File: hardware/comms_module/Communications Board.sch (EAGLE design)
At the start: 22 parts, among them U2 STC3115

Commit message: Add MUXes and moisture detection schematics.
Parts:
- added MCU: SABLE-X-BLE-MODULE, Capstone Library:SABLE-X-BLE-MODULE
- added MUX1: 74LV4051, Capstone Library:74LV4051
- added MUX2, U$3: 74LVC2G53, Capstone Library:74LVC2G53
- added Q1: MOSFET-PCHANNEL, SparkFun-DiscreteSemi:MOSFET-PCHANNEL
- added R1, R13, R14, R3: 4K32_0.1%, SparkFun-Passives:RESISTOR0603-RES
- U$1: value SABLE-X-BLE-MODULE -> 74LV4051; device Capstone Library:SABLE-X-BLE-MODULE -> Capstone Library:74LV4051
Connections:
- new net +1V3: MCU.DIO12, R14.1, R3.1
- new net +3V3: MCU.VCC, Q1.D
- new net BANDAGE_A_0: MCU.DIO11, MUX1.Y0, U$1.Y0
- new net BANDAGE_A_1: MUX1.Y1, U$1.Y1
- new net BANDAGE_A_2: MUX1.Y2, U$1.Y2
- new net BANDAGE_A_3: MUX1.Y3, U$1.Y3
- new net BANDAGE_A_4: MUX1.Y4, U$1.Y4
- new net BANDAGE_ID_0: U$1.Y5
- new net BANDAGE_ID_1: U$1.Y6
- new net CONN_STATE_RD: MCU.DIO4, MUX1.Z, MUX2.Z, U$1.Z, U$3.Z
- new net DBG_LED: U$1.Y7
- new net JTAG_TCKC: MCU.TCKC
- new net JTAG_TDI: MCU.DIO6/TDI
- new net JTAG_TDO: MCU.DIO5/TDO
- new net JTAG_TSMC: MCU.TSMC
- new net MCU_RST: MCU.RESET
- new net MPSW: MCU.DIO_0/BOOT_TX, MUX2.S, U$3.S
- new net MP_EN_SW: MCU.DIO9, MUX2./E, U$3./E
- new net MSW_0: MCU.DIO10, MUX1.S0, U$1.S0
- new net MSW_1: MCU.DIO8, MUX1.S1, U$1.S1
- new net MSW_2: MCU.DIO7, MUX1.S2, U$1.S2
- new net N$11: U$1.VEE
- new net PERIPHERAL_PWR: MCU.DIO1/BOOT_RX, Q1.G
- new net PERIPHERAL_VCC: MUX1.VCC, MUX2.VCC, Q1.S, R1.1, R13.1, U$1.VCC, U$3.VCC
- new net VSENSE_0: MCU.DIO14, MUX2.Y1, R1.2, R13.2, U$3.Y1
- new net VSENSE_1: MCU.DIO13, MUX2.Y0, R14.2, R3.2, U$3.Y0
- net GND: now also MCU.GND, MUX1./E, MUX1.GND, MUX1.VEE, MUX2.GND, U$1./E, U$1.GND, U$3.GND
- net SCL: now also MCU.DIO2
- net SDA: now also MCU.DIO3
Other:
- note added: "Close to R3"
- note added: "THIS MOSFET NOT YET SELECTED. VERIFY PKG."
- note added: "TP1"

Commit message: Add power management components.
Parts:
- removed MUX1: 74LV4051, Capstone Library:74LV4051
- removed MUX2: 74LVC2G53, Capstone Library:74LVC2G53
- removed R13, R14: 4K32_0.1%, SparkFun-Passives:RESISTOR0603-RES
- added C1, C3, C7, C8: (no value), SparkFun-Passives:CAP0603-CAP
- added L1: 1.5uH, SparkFun-Passives:INDUCTOR
- added U$4: TPS63031, Capstone Library:TPS63031
- added U$5: TLV717P, Capstone Library:TLV717P
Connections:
- new net N$10: C3.1, U$4.EN, U$4.PS/SYNC, U$4.VINA
- new net N$5: L1.1, U$4.L1
- new net N$8: L1.2, U$4.L2
- net +1V3: now also C8.1, U$5.VOUT; no longer R14.1
- net +3V3: now also C7.1, U$4.FB, U$4.VOUT
- net BANDAGE_A_0: no longer MUX1.Y0
- net BANDAGE_A_1: no longer MUX1.Y1
- net BANDAGE_A_2: no longer MUX1.Y2
- net BANDAGE_A_3: no longer MUX1.Y3
- net BANDAGE_A_4: no longer MUX1.Y4
- net CONN_STATE_RD: no longer MUX1.Z, MUX2.Z
- net GND: now also C1.2, C3.2, C7.2, C8.2, U$4.GND, U$4.PGND, U$5.GND; no longer MUX1./E, MUX1.GND, MUX1.VEE, MUX2.GND
- net MPSW: no longer MUX2.S
- net MP_EN_SW: no longer MUX2./E
- net MSW_0: no longer MUX1.S0
- net MSW_1: no longer MUX1.S1
- net MSW_2: no longer MUX1.S2
- net PERIPHERAL_VCC: now also U$5.EN, U$5.IN; no longer MUX1.VCC, MUX2.VCC, R13.1
- net VSENSE_0: no longer MUX2.Y1, R13.2
- net VSENSE_1: no longer MUX2.Y0, R14.2
- net V_PREBUCK: now also C1.1, U$4.VIN
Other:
- note added: "1V3 Regulator"
- note added: "3V3 Regulator"
- note added: "L1 not yet selected."
- note added: "Layout from TI Reference Design"
- note added: "Peripheral Power Disable"
- note added: "Place IN close to 3V3 reg."
- note removed: "TP1"
- moved on the sheet: MCU, Q1

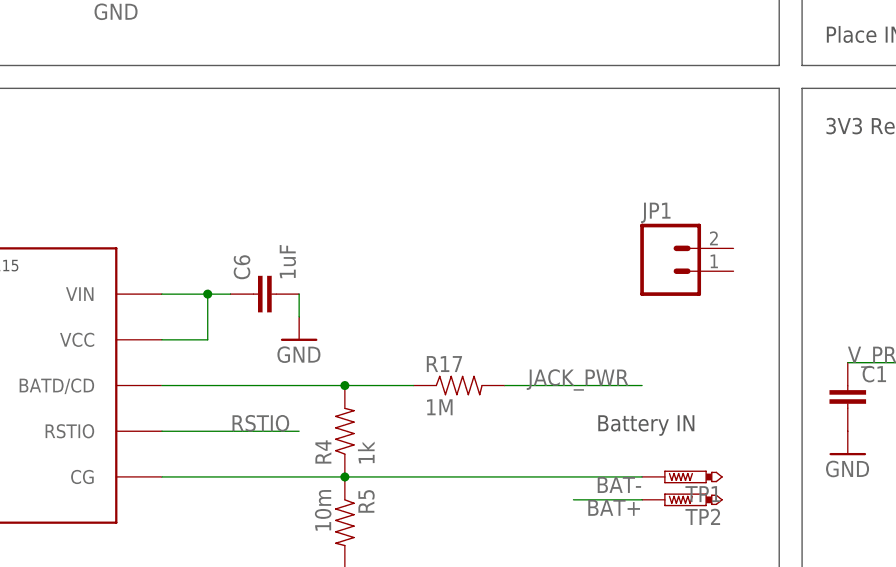
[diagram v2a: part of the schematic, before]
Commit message: Fix STC3115 Vcc connection
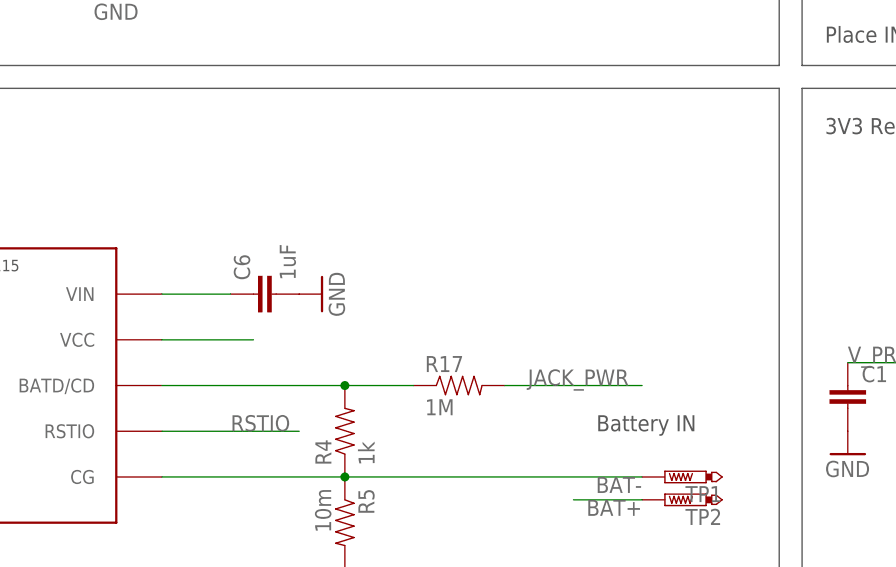
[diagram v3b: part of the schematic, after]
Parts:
- removed JP1: (no value), SparkFun-Connectors:M02JST-PTH-VERT
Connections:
- net N$6: no longer U2.VCC
- net VCC: now also U2.VCC
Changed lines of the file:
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@@
 <part name="SJ1" library="jumper" deviceset="SJ" device=""/>
 <part name="MCU" library="Capstone Library" deviceset="SABLE-X-BLE-MODULE" device=""/>
-<part name="JP1" library="SparkFun-Connectors" deviceset="M02" device="JST-PTH-VERT"/>
 <part name="TP1" library="testpad" deviceset="PTR1" device="TP16SQ"/>
 <part name="TP2" library="testpad" deviceset="PTR1" device="TP16SQ"/>
@@
 <instance part="GND15" gate="1" x="27.94" y="15.24"/>
 <instance part="C6" gate="G$1" x="78.74" y="40.64" rot="R90"/>
-<instance part="GND16" gate="1" x="81.28" y="35.56"/>
+<instance part="GND16" gate="1" x="83.82" y="40.64" rot="R90"/>
 <instance part="R4" gate="G$1" x="86.36" y="25.4" rot="R90"/>
 <instance part="R5" gate="G$1" x="86.36" y="15.24" rot="R270"/>
@@
 <instance part="SJ1" gate="1" x="25.4" y="106.68"/>
 <instance part="MCU" gate="G$1" x="353.06" y="116.84"/>
-<instance part="JP1" gate="G$1" x="121.92" y="43.18"/>
 <instance part="TP1" gate="G$1" x="121.92" y="20.32" rot="R90"/>
 <instance part="TP2" gate="G$1" x="121.92" y="17.78" rot="R90"/>
@@
 <pinref part="C6" gate="G$1" pin="2"/>
 <pinref part="GND16" gate="1" pin="GND"/>
-<wire x1="81.28" y1="38.1" x2="81.28" y2="40.64" width="0.1524" layer="91"/>
 </segment>
 <segment>
@@
 <net name="N$6" class="0">
 <segment>
-<pinref part="U2" gate="G$1" pin="VCC"/>
-<wire x1="66.04" y1="35.56" x2="71.12" y2="35.56" width="0.1524" layer="91"/>
-<wire x1="71.12" y1="35.56" x2="71.12" y2="40.64" width="0.1524" layer="91"/>
 <pinref part="U2" gate="G$1" pin="VIN"/>
-<wire x1="66.04" y1="40.64" x2="71.12" y2="40.64" width="0.1524" layer="91"/>
+<wire x1="66.04" y1="40.64" x2="73.66" y2="40.64" width="0.1524" layer="91"/>
 <pinref part="C6" gate="G$1" pin="1"/>
-<junction x="71.12" y="40.64"/>
-<wire x1="71.12" y1="40.64" x2="73.66" y2="40.64" width="0.1524" layer="91"/>
 </segment>
 </net>
@@
 <pinref part="P+1" gate="VCC" pin="VCC"/>
 </segment>
-</net>
+<segment>
+<pinref part="U2" gate="G$1" pin="VCC"/>
+<wire x1="66.04" y1="35.56" x2="76.2" y2="35.56" width="0.1524" layer="91"/>
+</segment>
+</net>

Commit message: Add remaining components and start board layout.
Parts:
- removed Q1: MOSFET-PCHANNEL, SparkFun-DiscreteSemi:MOSFET-PCHANNEL
- removed R10, R9: 1k, SparkFun-Passives:RESISTOR0603-RES
- removed SJ1: (no value), jumper:SJ
- added C10: 10uF, SparkFun-Passives:CAP0603-CAP
- added C9: 1uF, SparkFun-Passives:CAP0603-CAP
- added JP1, JP2: (no value), SparkFun-Connectors:M05X2NO_SILK
- added PSW: (no value), Capstone Library:SWITCH-SPDT
- added R13: 1Meg, SparkFun-Passives:RESISTOR0603-RES
- added R14, R16, R18: 100Meg, SparkFun-Passives:RESISTOR0603-RES
- added R15, R19: 10k, SparkFun-Passives:RESISTOR0603-RES
- added U$6, U$7, U$8: DMC2990UDJ, Capstone Library:DMC2990UDJ
- added X2: USB-MICROB, SparkFun:USB-MICROB
- C1, C7: value (none) -> 10uF
- C3: value (none) -> 0.1uF
- L1: device SparkFun-Passives:INDUCTOR -> Capstone Library:INDUCTOR
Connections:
- net BANDAGE_ID_0 renamed BANDAGE_DETECT
- removed net BANDAGE_ID_1: U$1.Y6
- removed net N$17: R9.1, U$2.PGOOD
- removed net N$18: R10.1, U$2.CHG
- removed net RSTIO: U2.RSTIO
- new net /SYSDISBL: C9.1, R15.1, U$1.Y6
- new net AGND: JP1.5, JP2.5
- new net BATDC: R17.1, R4.2, R6.2, U2.BATD/CD
- new net N$12: R13.1, U$6G$2.D
- new net N$13: JP1.8
- new net N$14: R14.1, R15.2, U$6G$2.G
- new net N$15: JP1.6
- new net N$16: JP1.3
- new net N$21: R16.2, U$7G$1.D
- new net N$22: R18.2, R19.2, U$6G$2.S, U$7G$1.G, U$7G$2.G
- new net N$25: JP2.9
- new net N$26: JP2.8
- new net N$27: JP2.6
- new net N$28: JP2.3
- new net N$29: JP2.1
- new net N$9: R13.2, U$6G$1.D, U$6G$1.G
- new net SYSOFF: R16.1, R6.1, U$2.SYSOFF, U$7G$2.D
- net +3V3: now also C10.1, R19.1, U$8G$2.S, U2.VCC; no longer Q1.D
- net BAT+: now also C6.1, PSW.P, R17.2, R18.1, U$7G$2.S, U2.VIN; no longer TP2.TP
- net BAT-: now also C5.2
- net GND: now also C10.2, C9.2, JP1.7, JP2.7, R14.2, U$6G$1.S, U$7G$1.S, X2.GND; no longer C5.2, R6.1
- net JACK_PWR: now also X2.VBUS; no longer R17.2, SJ1.1
- net MCU_RST: now also U2.RSTIO
- net N$19: now also JP1.1; no longer R6.2, SJ1.2, U$2.SYSOFF
- net N$6: now also PSW.S, TP2.TP; no longer C6.1, U2.VIN
- net N$7: now also JP1.9; no longer R17.1, R4.2, U2.BATD/CD
- net PERIPHERAL_PWR: now also U$8G$2.G; no longer Q1.G
- net PERIPHERAL_VCC: now also JP1.10, JP2.10, U$8G$2.D; no longer Q1.S
- net SCL: now also JP1.2, JP2.2
- net SDA: now also JP1.4, JP2.4
- net VCC: no longer U2.VCC
- net V_PREBUCK: no longer R10.2, R9.2
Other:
- note added: "ADD CHG/PGOOD LEDs if space Available"
- note added: "Battery Power Disable"
- note removed: "L1 not yet selected."
- note removed: "THIS MOSFET NOT YET SELECTED. VERIFY PKG."
- moved on the sheet: C6, MCU, R6, TP2

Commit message: Continued routing of the communications board.
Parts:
- removed PSW: (no value), Capstone Library:SWITCH-SPDT
- removed TP1, TP2: PTR1TP16SQ, testpad:PTR1TP16SQ
- added B_CONN, B_EN: (no value), SparkFun-Connectors:M02PTH
- added JP3, JP4: (no value), SparkFun-Connectors:M021X02_NO_SILK
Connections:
- removed net N$6: PSW.S, TP2.TP
- new net B+IN: B_CONN.1, B_EN.1
- net +3V3: now also JP3.1, JP4.1
- net BAT+: now also B_EN.2; no longer PSW.P
- net BAT-: now also B_CONN.2; no longer TP1.TP
- net V_PREBUCK: now also JP3.2, JP4.2
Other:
- note added: "Top-Bottom Board Power Passthrough"
- note removed: "Battery IN"
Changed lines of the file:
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@@
 <part name="R17" library="SparkFun-Passives" deviceset="RESISTOR" device="0603-RES" value="1M"/>
 <part name="MCU" library="Capstone Library" deviceset="SABLE-X-BLE-MODULE" device=""/>
-<part name="TP1" library="testpad" deviceset="PTR1" device="TP16SQ"/>
-<part name="TP2" library="testpad" deviceset="PTR1" device="TP16SQ"/>
 <part name="+3V1" library="supply1" deviceset="+3V3" device=""/>
 <part name="GND1" library="supply1" deviceset="GND" device=""/>
@@
 <part name="+3V4" library="supply1" deviceset="+3V3" device=""/>
 <part name="+3V5" library="supply1" deviceset="+3V3" device=""/>
-<part name="PSW" library="Capstone Library" deviceset="SWITCH-SPDT" device=""/>
 <part name="JP1" library="SparkFun-Connectors" deviceset="M05X2" device="NO_SILK"/>
 <part name="GND3" library="supply1" deviceset="GND" device=""/>
@@
 <part name="X2" library="SparkFun" deviceset="USB" device="-MICROB"/>
 <part name="GND22" library="SparkFun" deviceset="GND" device=""/>
+<part name="B_EN" library="SparkFun-Connectors" deviceset="M02" device="PTH"/>
+<part name="B_CONN" library="SparkFun-Connectors" deviceset="M02" device="PTH"/>
+<part name="JP3" library="SparkFun-Connectors" deviceset="M02" device="1X02_NO_SILK"/>
+<part name="+3V6" library="supply1" deviceset="+3V3" device=""/>
+<part name="JP4" library="SparkFun-Connectors" deviceset="M02" device="1X02_NO_SILK"/>
+<part name="+3V7" library="supply1" deviceset="+3V3" device=""/>
 </parts>
 <sheets>
@@
 <wire x1="134.62" y1="167.64" x2="83.82" y2="167.64" width="0.1524" layer="97"/>
 <text x="86.36" y="198.12" size="1.778" layer="97">I2C Pullups</text>
-<text x="114.3" y="22.86" size="1.778" layer="97">Battery IN</text>
 <text x="147.32" y="190.5" size="1.778" layer="97">Next steps:
  - Make the component for the buck/boost
@@
 <text x="236.22" y="81.28" size="1.778" layer="97">Battery Power Disable </text>
 <text x="35.56" y="139.7" size="1.778" layer="97">ADD CHG/PGOOD LEDs if space Available</text>
+<text x="360.68" y="50.8" size="1.778" layer="97">Top-Bottom Board Power Passthrough</text>
 </plain>
 <instances>
@@
 <instance part="R17" gate="G$1" x="99.06" y="30.48"/>
 <instance part="MCU" gate="G$1" x="320.04" y="172.72"/>
-<instance part="TP1" gate="G$1" x="121.92" y="20.32" rot="R90"/>
-<instance part="TP2" gate="G$1" x="124.46" y="10.16" rot="R90"/>
 <instance part="+3V1" gate="G$1" x="259.08" y="193.04"/>
 <instance part="GND1" gate="1" x="259.08" y="182.88"/>
@@
 <instance part="+3V4" gate="G$1" x="236.22" y="66.04" rot="R90"/>
 <instance part="+3V5" gate="G$1" x="83.82" y="35.56" rot="R270"/>
-<instance part="PSW" gate="1" x="114.3" y="12.7"/>
 <instance part="JP1" gate="G$1" x="378.46" y="20.32"/>
 <instance part="GND3" gate="1" x="360.68" y="12.7"/>
@@
 <instance part="X2" gate="G$1" x="10.16" y="81.28" rot="R180"/>
 <instance part="GND22" gate="1" x="38.1" y="78.74"/>
+<instance part="B_EN" gate="G$1" x="114.3" y="12.7" rot="R180"/>
+<instance part="B_CONN" gate="G$1" x="127" y="22.86" rot="R180"/>
+<instance part="JP3" gate="G$1" x="375.92" y="40.64"/>
+<instance part="+3V6" gate="G$1" x="406.4" y="40.64" rot="R270"/>
+<instance part="JP4" gate="G$1" x="464.82" y="40.64"/>
+<instance part="+3V7" gate="G$1" x="495.3" y="40.64" rot="R270"/>
 </instances>
 <busses>
@@
 <label x="142.24" y="33.02" size="1.778" layer="95"/>
 </segment>
+<segment>
+<pinref part="JP3" gate="G$1" pin="2"/>
+<wire x1="383.54" y1="43.18" x2="398.78" y2="43.18" width="0.1524" layer="91"/>
+<label x="383.54" y="43.18" size="1.778" layer="95"/>
+</segment>
+<segment>
+<pinref part="JP4" gate="G$1" pin="2"/>
+<wire x1="472.44" y1="43.18" x2="487.68" y2="43.18" width="0.1524" layer="91"/>
+<label x="472.44" y="43.18" size="1.778" layer="95"/>
+</segment>
 </net>
 <net name="JACK_PWR" class="0">
@@
 </segment>
 <segment>
-<pinref part="PSW" gate="1" pin="P"/>
-<wire x1="111.76" y1="12.7" x2="106.68" y2="12.7" width="0.1524" layer="91"/>
-<label x="106.68" y="12.7" size="1.778" layer="95"/>
+<pinref part="B_EN" gate="G$1" pin="2"/>
+<wire x1="106.68" y1="10.16" x2="96.52" y2="10.16" width="0.1524" layer="91"/>
+<label x="96.52" y="10.16" size="1.778" layer="95"/>
 </segment>
 </net>
@@
 <net name="BAT-" class="0">
 <segment>
-<label x="106.68" y="17.78" size="1.778" layer="95"/>
+<label x="106.68" y="20.32" size="1.778" layer="95"/>
 <pinref part="R4" gate="G$1" pin="1"/>
 <pinref part="U2" gate="G$1" pin="CG"/>
@@
 <junction x="86.36" y="20.32"/>
 <wire x1="119.38" y1="20.32" x2="86.36" y2="20.32" width="0.1524" layer="91"/>
-<pinref part="TP1" gate="G$1" pin="TP"/>
+<pinref part="B_CONN" gate="G$1" pin="2"/>
 </segment>
 <segment>
@@
 <pinref part="+3V5" gate="G$1" pin="+3V3"/>
 </segment>
+<segment>
+<pinref part="JP3" gate="G$1" pin="1"/>
+<wire x1="383.54" y1="40.64" x2="403.86" y2="40.64" width="0.1524" layer="91"/>
+<pinref part="+3V6" gate="G$1" pin="+3V3"/>
+<label x="383.54" y="40.64" size="1.778" layer="95"/>
+</segment>
+<segment>
+<pinref part="JP4" gate="G$1" pin="1"/>
+<wire x1="472.44" y1="40.64" x2="492.76" y2="40.64" width="0.1524" layer="91"/>
+<pinref part="+3V7" gate="G$1" pin="+3V3"/>
+<label x="472.44" y="40.64" size="1.778" layer="95"/>
+</segment>
 </net>
 <net name="MCU_RST" class="0">
@@
 </segment>
 </net>
-<net name="N$6" class="0">
-<segment>
-<pinref part="PSW" gate="1" pin="S"/>
-<pinref part="TP2" gate="G$1" pin="TP"/>
-<wire x1="119.38" y1="10.16" x2="121.92" y2="10.16" width="0.1524" layer="91"/>
-</segment>
-</net>
+<net name="B+IN" class="0">
+<segment>
+<pinref part="B_CONN" gate="G$1" pin="1"/>
+<wire x1="119.38" y1="22.86" x2="106.68" y2="22.86" width="0.1524" layer="91"/>
+<label x="106.68" y="22.86" size="1.778" layer="95"/>
+</segment>
+<segment>
+<pinref part="B_EN" gate="G$1" pin="1"/>
+<wire x1="106.68" y1="12.7" x2="96.52" y2="12.7" width="0.1524" layer="91"/>
+<label x="96.52" y="12.7" size="1.778" layer="95"/>
+</segment>
+</net>

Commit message: Continued routing of top and bottom.
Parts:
- added JP5, JP6: (no value), SparkFun-Connectors:M01PTH
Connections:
- removed net N$11: U$1.VEE
- removed net N$13: JP1.8
- removed net N$14: R14.1, R15.2, U$6G$2.G
- removed net N$15: JP1.6
- removed net N$16: JP1.3
- removed net N$19: JP1.1
- removed net N$7: JP1.9
- removed net VCC: R11.2, R12.2
- new net SYSDPASS: JP5.1, JP6.1, R14.1, R15.2, U$6G$2.G
- net +3V3: now also R11.2, R12.2
- net BANDAGE_A_0: now also JP1.6
- net BANDAGE_A_1: now also JP1.3
- net BANDAGE_A_2: now also JP1.8
- net BANDAGE_A_3: now also JP1.1
- net BANDAGE_A_4: now also JP1.9
- net GND: now also U$1.VEE
- net MSW_0: now also MCU.DIO7; no longer MCU.DIO10
- net MSW_2: now also MCU.DIO10; no longer MCU.DIO7
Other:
- moved on the sheet: R13, R16, R18, R6, U$6G$1, U$6G$2, U$7G$1, U$7G$2

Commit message: Convert to 4 layer. Nearly complete routing.
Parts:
- removed JP1, JP2: (no value), SparkFun-Connectors:M05X2NO_SILK
- removed MCU: SABLE-X-BLE-MODULE, Capstone Library:SABLE-X-BLE-MODULE
- added C11, C12: 1.2pF, SparkFun-Passives:CAP0402-CAP
- added C13, C23, C24: 12pF, SparkFun-Passives:CAP0402-CAP
- added C14: 1uF, SparkFun-Passives:CAP0402-CAP
- added C15, C16, C17, C19, C21, C22: 100nF, SparkFun-Passives:CAP0402-CAP
- added C18, C20: 10uF, SparkFun-Passives:CAP0402-CAP
- added FL1: BLM18HE152SN1, Michael Blouin Library:INDUCTOR0603
- added JP7, JP8: 2X6 FEMALE, SparkFun-Connectors:M06X2PTH_FEMALE
- added L2: 2nH, SparkFun-Passives:INDUCTOR0402
- added L3: 15nH, SparkFun-Passives:INDUCTOR0402
- added L4: 10uH, Michael Blouin Library:INDUCTOR0603
- added R9: 100k, SparkFun-Passives:RESISTOR0603-RES
- added U1: Value, Capstone Library:CC2640F128RHBR
- added Y1: 32.768kHz, Capstone Library:CRYSTAL
- added Y2: 24MHz, Capstone Library:CRYSTAL-GROUNDED
- C1, C3, C7, C8: device SparkFun-Passives:CAP0603-CAP -> SparkFun-Passives:CAP0402-CAP
- R1, R3: device SparkFun-Passives:RESISTOR0603-RES -> SparkFun-Passives:RESISTOR0402-RES
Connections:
- removed net BANDAGE_DETECT: U$1.Y5
- removed net SYSDPASS: JP5.1, JP6.1, R14.1, R15.2, U$6G$2.G
- new net ANTENNA: C13.2
- new net DCDC_SW: L4.1, U1.DCDC_SW
- new net N$18: C23.1, U1.X32K_Q2, Y1.1
- new net N$19: C24.1, U1.X32K_Q1, Y1.2
- new net N$41: C12.1, C13.1, L2.2
- new net N$43: C14.1, U1.DCOUPL
- new net PERIPHERAL_DETECT: JP7.12, JP8.12, U$1.Y5
- new net RF_N: L3.1, U1.RF_N
- new net RF_P: C11.1, L2.1, L3.2, U1.RF_P
- new net VCC: C16.1, C17.1, C18.1, C19.1, FL1.2, R9.2, U1.VDDS, U1.VDDS2, U1.VDDS_DCDC
- new net VDDR: C20.1, C21.1, C22.1, L4.2, U1.VDDR, U1.VDDR_RF
- new net X24M_N: U1.X24M_N, Y2.2
- new net X24M_P: U1.X24M_P, Y2.1
- net +1V3: now also U1.DIO_9; no longer MCU.DIO12
- net +3V3: now also FL1.1; no longer MCU.VCC
- net /SYSDISBL: now also JP5.1, JP6.1, R14.1, R15.2, U$6G$2.G
- net AGND: now also JP8.5; no longer JP1.5, JP2.5
- net BANDAGE_A_0: now also JP7.6, U$1.Y3, U1.DIO_10; no longer JP1.6, MCU.DIO11, U$1.Y0
- net BANDAGE_A_1: now also JP7.3, U$1.Y2; no longer JP1.3, U$1.Y1
- net BANDAGE_A_2: now also JP7.8, U$1.Y1; no longer JP1.8, U$1.Y2
- net BANDAGE_A_3: now also JP7.1, U$1.Y0; no longer JP1.1, U$1.Y3
- net BANDAGE_A_4: now also JP7.9; no longer JP1.9
- net CONN_STATE_RD: now also U1.DIO_12; no longer MCU.DIO4
- net GND: now also C11.2, C12.2, C14.2, C15.2, C16.2, C17.2, C18.2, C19.2, C20.2, C21.2, C22.2, C23.2, C24.2, JP7.5, JP7.7, JP8.7, U1.VSS, Y2.3; no longer JP1.7, JP2.7, MCU.GND
- net JTAG_TCKC: now also U1.JTAG_TCKC; no longer MCU.TCKC
- net JTAG_TDI: now also U1.DIO_6; no longer MCU.DIO6/TDI
- net JTAG_TDO: now also U1.DIO_5; no longer MCU.DIO5/TDO
- net JTAG_TSMC: now also U1.JTAG_TMSC; no longer MCU.TSMC
- net MCU_RST: now also C15.1, R9.1, U1.RESET_N; no longer MCU.RESET
- net MPSW: now also U1.DIO_4; no longer MCU.DIO_0/BOOT_TX
- net MP_EN_SW: now also U1.DIO_0; no longer MCU.DIO9
- net MSW_0: now also U1.DIO_1; no longer MCU.DIO7
- net MSW_1: now also U1.DIO_2; no longer MCU.DIO8
- net MSW_2: now also U1.DIO_3; no longer MCU.DIO10
- net N$25: now also JP8.9; no longer JP2.9
- net N$26: now also JP8.8; no longer JP2.8
- net N$27: now also JP8.6; no longer JP2.6
- net N$28: now also JP8.3; no longer JP2.3
- net N$29: now also JP8.1; no longer JP2.1
- net PERIPHERAL_PWR: now also U1.DIO_11; no longer MCU.DIO1/BOOT_RX
- net PERIPHERAL_VCC: now also JP7.10, JP7.11, JP8.10, JP8.11; no longer JP1.10, JP2.10
- net SCL: now also JP7.2, JP8.2, U1.DIO_14; no longer JP1.2, JP2.2, MCU.DIO2
- net SDA: now also JP7.4, JP8.4, U1.DIO_13; no longer JP1.4, JP2.4, MCU.DIO3
- net VSENSE_0: now also U1.DIO_7; no longer MCU.DIO14
- net VSENSE_1: now also U1.DIO_8; no longer MCU.DIO13
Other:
- note added: "L3 Can be removed"
- note added: "NC"
- note added: "VCC is for MCU high-frequency domain and is seperated by a GHz noise filter from 3.3V."
- note added: "Verify size of inductor 0402 package."
- note removed: "Next steps: - Make the component for the buck/boost - Look at installing a resetable fuse inside - Add RGB LED - Determine the connector required"
